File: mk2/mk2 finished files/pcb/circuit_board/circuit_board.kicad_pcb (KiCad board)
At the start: 2 copper layers, 50.8 x 34.3 mm, 13 parts, among them J1 2x3 Header, Q1 IRLZ44N, U1 ATtiny1614, U2 L7805

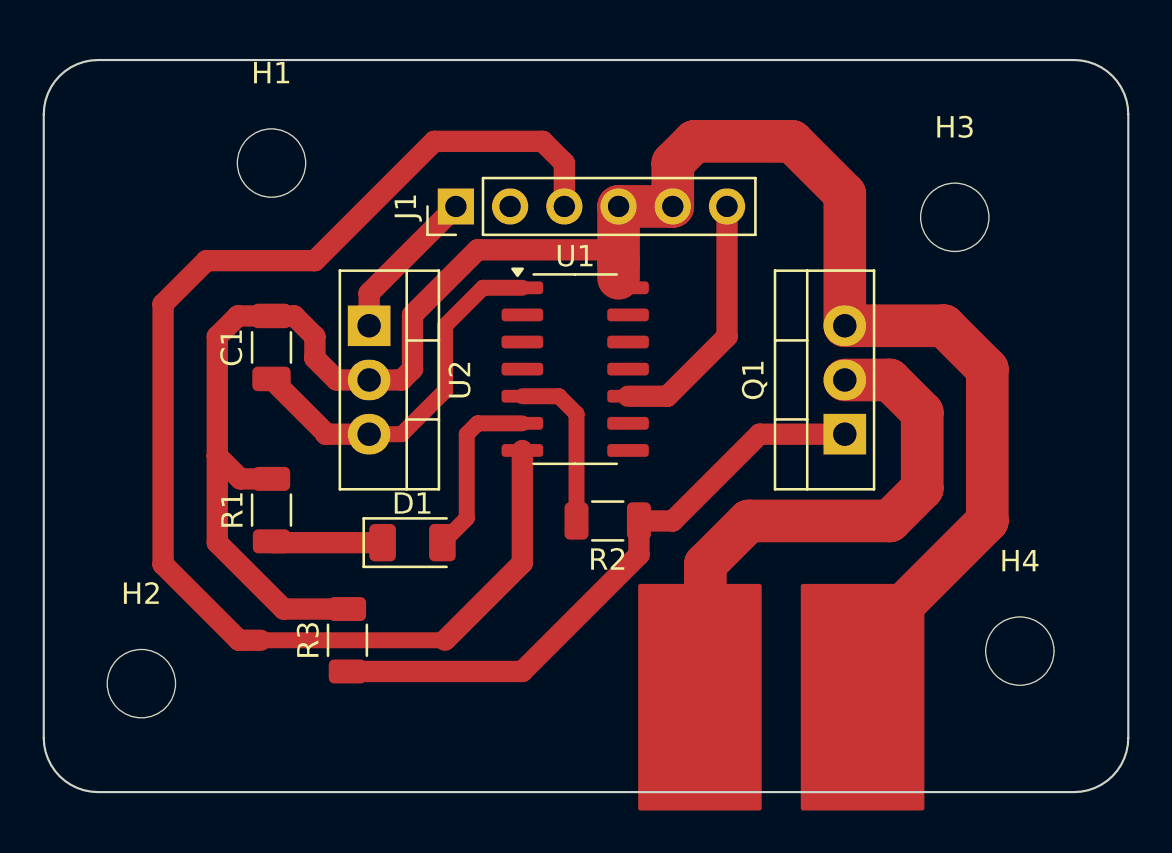
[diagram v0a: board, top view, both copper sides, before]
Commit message: PCB Pinout Rework
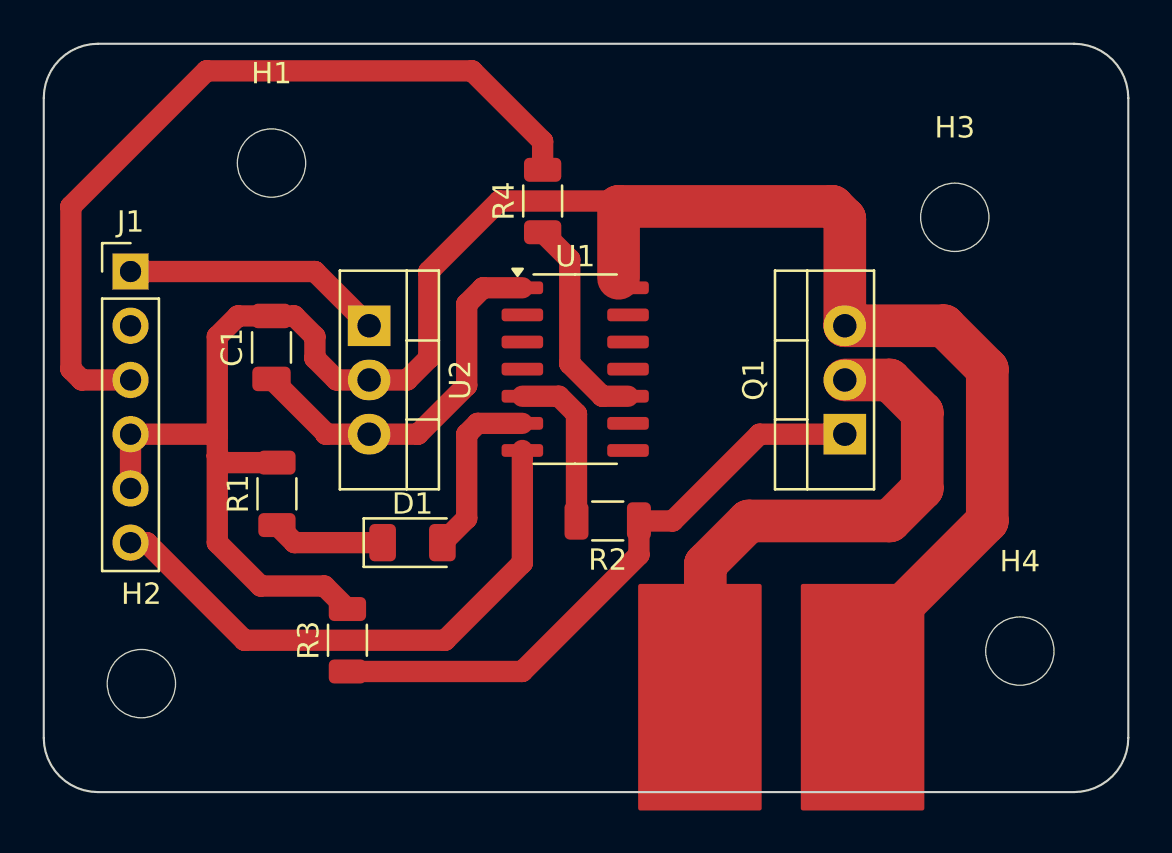
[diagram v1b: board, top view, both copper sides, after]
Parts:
- added R4: 0Ω, Resistor_SMD:R_1206_3216Metric, F.Cu at (206.2, 109.5)
- moved J1 15.5 mm to (186.9, 112.8), turned to 0 degrees
- moved R1 0.80 mm to (193.8, 123.2)
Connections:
- U1 pad 10: Net-(J1-Pin_6) -> Net-(U1-PA0//UPDI)
- U1 pad 7: Net-(J1-Pin_3) -> Net-(J1-Pin_6)
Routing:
- net Net-(J1-Pin_3): track 61.7 -> 38.1 mm
- net Net-(J1-Pin_6): track 11.9 -> 27.0 mm
- net Net-(U1-PA0//UPDI): track 0.00 -> 10.0 mm
- net Net-(J1-Pin_1): track 7.27 -> 12.2 mm
- net Net-(J1-Pin_4): track 91.3 -> 95.9 mm
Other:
- board size 50.8 x 34.3 mm -> 50.8 x 35.1 mm
